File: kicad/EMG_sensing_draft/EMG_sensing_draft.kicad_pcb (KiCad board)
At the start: 2 copper layers, 49.4 x 60.1 mm, 157 parts, among them J1 USB_A_0480370001, J2 Conn_01x09, J3 DEBUG, U1 MCP6N11-002E/SN, U10 RP2040, U11 RN4871-I/RM140, U12 MCP1702T-3302E_CB, U13 Opamp_MCP6024T-E/ST, U14 Opamp_MCP6024T-E/ST, U15 Opamp_MCP6024T-E/ST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

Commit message: Fix layout issues
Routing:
- net Net-(R1-Pad1): track 38.4 -> 40.8 mm
- net GND: track 449.5 -> 450.9 mm
- net Net-(R68-Pad2): track 4.48 -> 5.39 mm
- net Net-(R67-Pad2): track 4.40 -> 5.24 mm
- net Net-(R25-Pad2): track 7.58 -> 8.40 mm
- net Net-(D13-Pad1): track 4.76 -> 5.54 mm
- net Net-(C28-Pad2): track 9.40 -> 8.63 mm
- net Net-(D13-Pad2): track 6.58 -> 7.26 mm
- net +1.65V: track 253.1 -> 253.8 mm
- net Net-(C36-Pad2): track 16.5 -> 17.1 mm

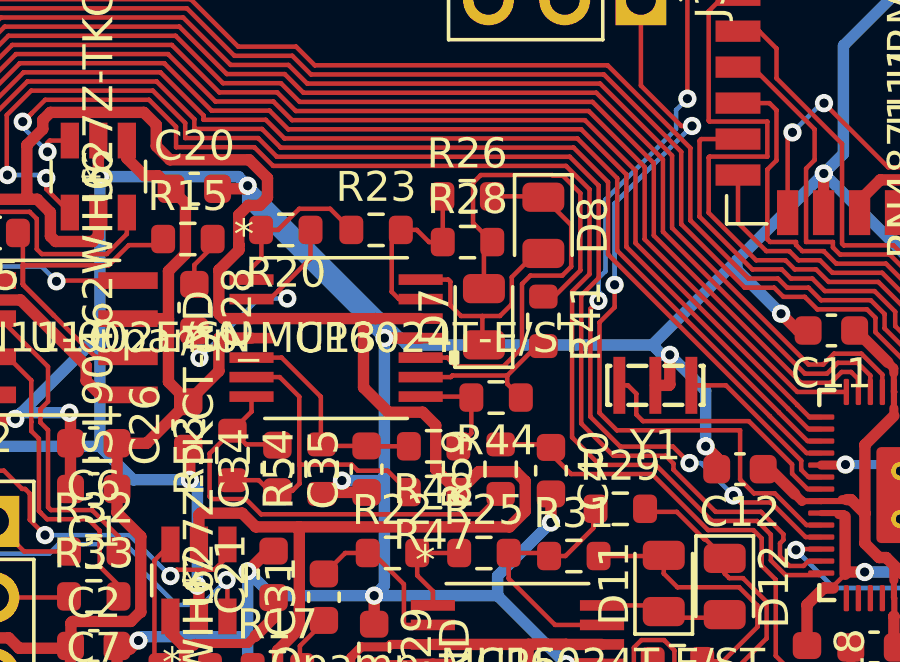
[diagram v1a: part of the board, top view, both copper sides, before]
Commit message: removed references from silkscreen
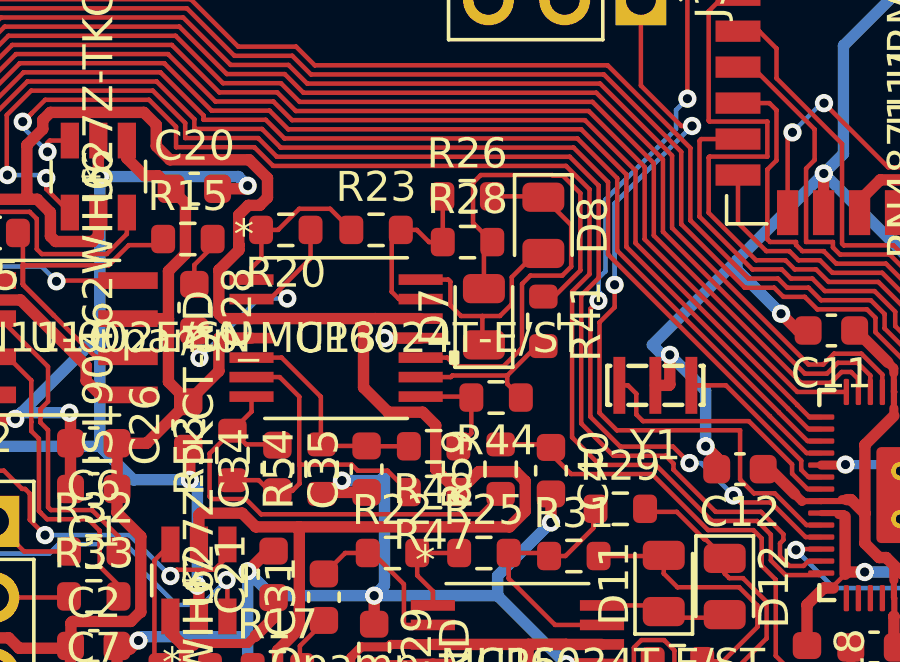
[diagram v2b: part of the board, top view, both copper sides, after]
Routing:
- net GND: track 450.9 -> 423.7 mm
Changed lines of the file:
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@@
   (segment (start 247.0404 47.3964) (end 245.2624 49.1744) (width 0.381) (layer "B.Cu") (net 2))
   (segment (start 243.083746 63.186665) (end 242.297347 62.400266) (width 0.381) (layer "B.Cu") (net 2))
-  (segment (start 242.23842 41.4777) (end 236.93076 36.17004) (width 0.381) (layer "B.Cu") (net 2))
   (segment (start 241.1476 49.8348) (end 241.49 49.4924) (width 0.381) (layer "B.Cu") (net 2))
   (segment (start 268.0716 44.0944) (end 264.4648 44.0944) (width 0.381) (layer "B.Cu") (net 2))
@@
   (segment (start 229.1847 43.942) (end 231.6231 41.5036) (width 0.381) (layer "B.Cu") (net 2))
   (segment (start 233.289299 51.330407) (end 233.413306 51.2064) (width 0.381) (layer "B.Cu") (net 2))
-  (segment (start 241.49 45.8592) (end 241.49 41.2496) (width 0.381) (layer "B.Cu") (net 2))
   (segment (start 251.0028 41.8084) (end 250.7498 41.8084) (width 0.381) (layer "B.Cu") (net 2))
   (segment (start 247.0404 53.4416) (end 247.9548 52.5272) (width 0.3048) (layer "B.Cu") (net 2))
@@
   (segment (start 253.238 38.6588) (end 250.4191 41.4777) (width 0.381) (layer "B.Cu") (net 2))
   (segment (start 233.4768 64.2869) (end 236.5629 64.2869) (width 0.381) (layer "B.Cu") (net 2))
-  (segment (start 250.4191 41.4777) (end 242.23842 41.4777) (width 0.381) (layer "B.Cu") (net 2))
-  (segment (start 241.49 41.2496) (end 236.93076 36.69036) (width 0.381) (layer "B.Cu") (net 2))
   (segment (start 233.413306 51.2064) (end 236.9312 51.2064) (width 0.381) (layer "B.Cu") (net 2))
   (segment (start 235.2548 49.5041) (end 235.2548 46.228) (width 0.381) (layer "B.Cu") (net 2))
@@
   (segment (start 269.5956 78.6892) (end 249.8852 78.6892) (width 0.381) (layer "B.Cu") (net 2))
   (segment (start 265.43 51.9684) (end 268.0716 49.3268) (width 0.381) (layer "B.Cu") (net 2))
-  (segment (start 236.93076 36.69036) (end 236.93076 36.17004) (width 0.381) (layer "B.Cu") (net 2))
   (segment (start 235.2548 46.228) (end 235.0008 45.974) (width 0.381) (layer "B.Cu") (net 2))
   (segment (start 262.9239 48.282) (end 262.404 48.282) (width 0.2032) (layer "F.Cu") (net 3))
@@
   (segment (start 246.933001 74.822601) (end 245.384733 74.822601) (width 0.1524) (layer "F.Cu") (net 140))
   (segment (start 243.4336 73.257801) (end 242.758598 72.582799) (width 0.1524) (layer "F.Cu") (net 140))
-  (zone (net 2) (net_name "GND") (layer "B.Cu") (hatch edge 0.508)
+  (zone locked (net 2) (net_name "GND") (layer "B.Cu") (hatch edge 0.508)
     (connect_pads (clearance 0.508))
     (min_thickness 0.254) (filled_areas_thickness no)

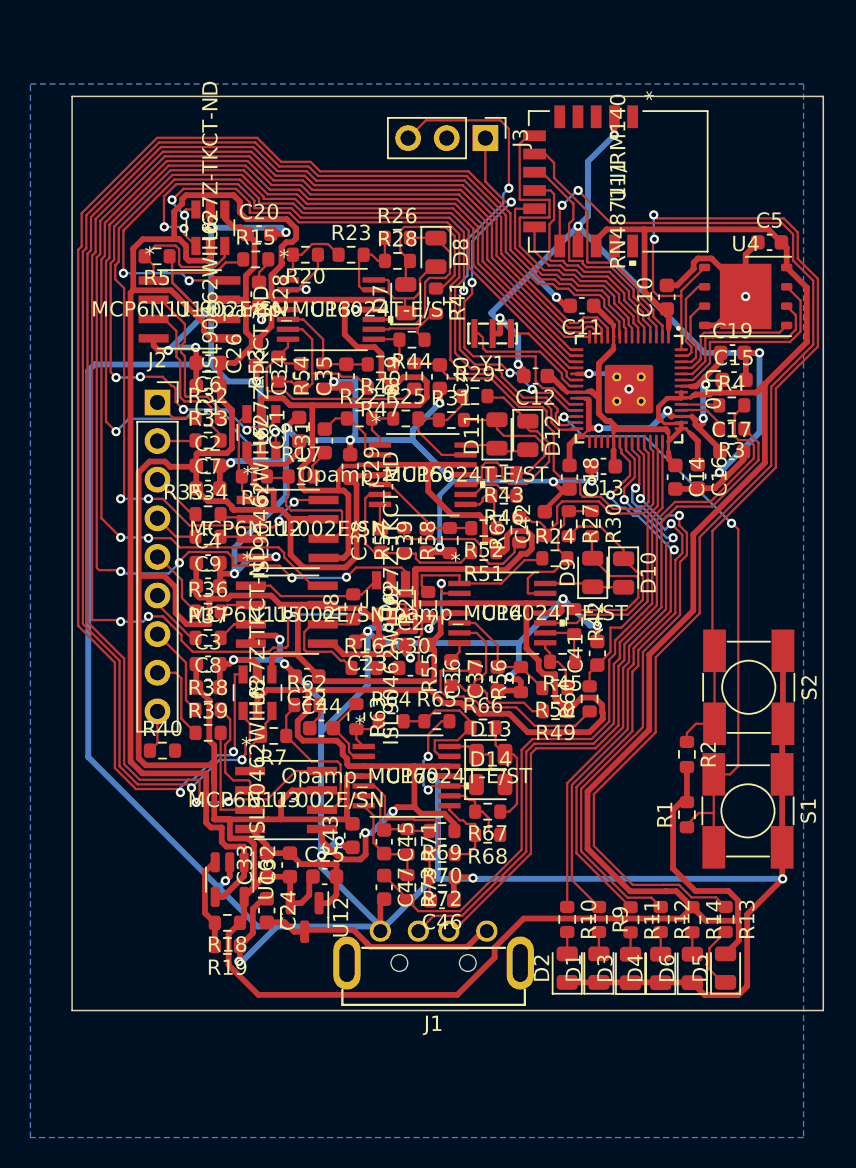
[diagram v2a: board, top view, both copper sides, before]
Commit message: removed references
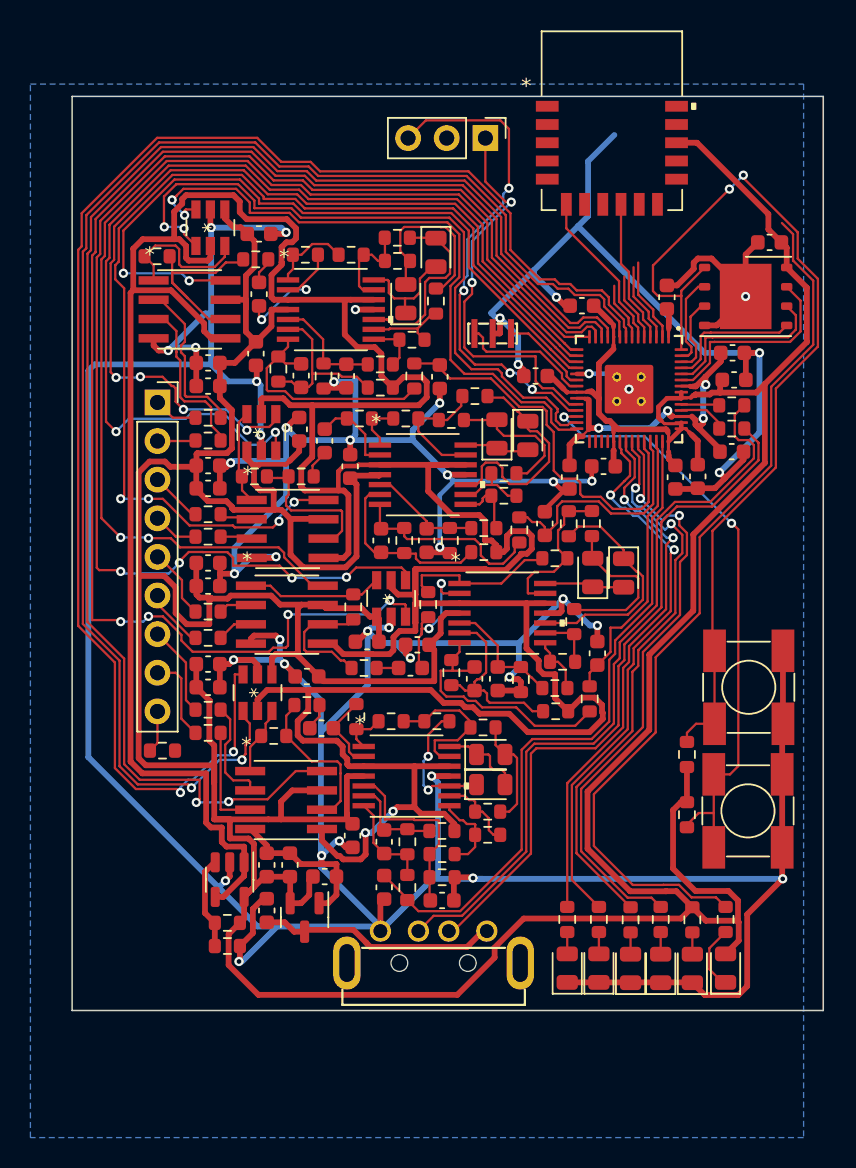
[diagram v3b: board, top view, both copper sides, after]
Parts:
- moved U11 4.01 mm to (258.4, 28.8), turned to 0 degrees
- renumbered J3 to J
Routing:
- net Net-(R13-Pad1): track 76.6 -> 58.1 mm, vias 2 -> 0
- net /RX_IND: track 23.0 -> 10.7 mm
- net /BLE_RX: track 16.9 -> 5.55 mm
- net /RST_N: track 14.8 -> 3.85 mm
- net /BLE_TX: track 16.2 -> 5.20 mm
- net +3.3V: track 357.3 -> 348.2 mm
- net /CTS: track 12.1 -> 4.51 mm
- net /RTS: track 15.5 -> 9.51 mm
- net GND: track 423.7 -> 421.1 mm, vias 44 -> 42

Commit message: finished four layer layout
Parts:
- moved J3 16.8 mm to (233.5, 32.8)
- moved C3 15.5 mm to (241.0, 77.0)
- moved C8 12.1 mm to (240.2, 74.7), turned to -90 degrees
- moved C4 7.47 mm to (235.9, 64.2), turned to 180 degrees
- moved C20 7.23 mm to (228.2, 38.2), turned to 180 degrees
- moved D10 7.01 mm to (253.8, 63.1), turned to 90 degrees
- moved R15 6.81 mm to (228.3, 36.3)
- moved R23 6.80 mm to (234.7, 35.8)
- moved R28 6.66 mm to (237.7, 36.9)
- moved R26 6.63 mm to (237.7, 35.4)
- moved C9 6.62 mm to (238.3, 60.8), turned to -90 degrees
- moved D8 6.50 mm to (241.0, 34.5), turned to 0 degrees
- moved C28 6.05 mm to (231.4, 35.5), turned to 0 degrees
- moved U11 5.99 mm to (253.4, 32.1)
- moved C29 5.93 mm to (237.6, 56.3), turned to 90 degrees
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- renumbered J to J3
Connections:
- U10 pad 11: /DIF_AMP_FOUR_CAL -> Net-(R9-Pad1)
- U10 pad 12: /POT_CHANGE_THREE -> Net-(R10-Pad1)
- U10 pad 13: /POT_CS_THREE -> Net-(R11-Pad1)
- U10 pad 14: /DIF_AMP_THREE_CAL -> Net-(R12-Pad1)
- U10 pad 29: unconnected-(U10-Pad29) -> /DIF_AMP_THREE_CAL
- U10 pad 30: unconnected-(U10-Pad30) -> /POT_CS_THREE
- U10 pad 31: unconnected-(U10-Pad31) -> /POT_CHANGE_THREE
- U10 pad 34: Net-(R9-Pad1) -> unconnected-(U10-Pad34)
- U10 pad 35: Net-(R10-Pad1) -> /DIF_AMP_FOUR_CAL
- U10 pad 36: Net-(R11-Pad1) -> /POT_CS_FOUR
- U10 pad 37: Net-(R12-Pad1) -> /POT_CHANGE_FOUR
- U10 pad 8: /POT_CHANGE_FOUR -> unconnected-(U10-Pad8)
- U10 pad 9: /POT_CS_FOUR -> unconnected-(U10-Pad9)
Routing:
- net GND: track 421.1 -> 114.5 mm, vias 42 -> 40
- net +3.3V: track 348.2 -> 102.3 mm, vias 0 -> 19
- net /POT_CHANGE_THREE: track 94.3 -> 26.1 mm
- net /POT_CS_THREE: track 87.2 -> 23.4 mm
- net +1.65V: track 253.8 -> 192.4 mm
- net /DIF_AMP_THREE_CAL: track 75.8 -> 26.6 mm
- net /DIF_AMP_TWO_CAL: track 71.4 -> 25.4 mm
- net /POT_CHANGE_TWO: track 66.3 -> 22.1 mm
- net /POT_CS_TWO: track 61.8 -> 25.4 mm, vias 4 -> 2
- net Net-(R10-Pad1): track 35.8 -> 56.3 mm
- net Net-(R12-Pad1): track 39.2 -> 59.6 mm
- net Net-(R11-Pad1): track 37.7 -> 58.0 mm
- net Net-(R9-Pad1): track 37.1 -> 56.1 mm
- net Net-(R2-Pad1): track 61.8 -> 43.3 mm
- net /POT_CHANGE_ONE: track 42.6 -> 24.8 mm
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- added copper zone on In2.Cu, net +3.3V
- added copper zone on In1.Cu, net GND
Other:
- copper layers 2 -> 4

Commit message: added silkscreen labels and fixed drc issues
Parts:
- added kibuzzard-63775D6F: G***, kibuzzard-63775D6F, F.Cu at (255.4, 86.7)
- added kibuzzard-63775D95: G***, kibuzzard-63775D95, F.Cu at (257.5, 86.7)
- added kibuzzard-63775DA9: G***, kibuzzard-63775DA9, F.Cu at (259.6, 86.7)
- added kibuzzard-63775DCC: G***, kibuzzard-63775DCC, F.Cu at (261.6, 86.7)
- added kibuzzard-63775DF3: G***, kibuzzard-63775DF3, F.Cu at (263.7, 86.7)
- added kibuzzard-63775E08: G***, kibuzzard-63775E08, F.Cu at (265.8, 86.7)
- added kibuzzard-63775E2B: G***, kibuzzard-63775E2B, F.Cu at (226.6, 52.4)
- added kibuzzard-63775E55: G***, kibuzzard-63775E55, F.Cu at (226.6, 54.8)
- added kibuzzard-63775E69: G***, kibuzzard-63775E69, F.Cu at (226.6, 57.4)
- added kibuzzard-63775E81: G***, kibuzzard-63775E81, F.Cu at (226.6, 59.9)
- added kibuzzard-63775ECF: G***, kibuzzard-63775ECF, F.Cu at (226.6, 62.5)
- added kibuzzard-63775F11: G***, kibuzzard-63775F11, F.Cu at (226.6, 65.0)
- added kibuzzard-63775F30: G***, kibuzzard-63775F30, F.Cu at (226.6, 67.6)
- added kibuzzard-63775F41: G***, kibuzzard-63775F41, F.Cu at (226.6, 70.2)
- added kibuzzard-63775F53: G***, kibuzzard-63775F53, F.Cu at (226.6, 72.6)
- added kibuzzard-63775F9D: G***, kibuzzard-63775F9D, F.Cu at (267.1, 65.2)
- added kibuzzard-63775FC8: G***, kibuzzard-63775FC8, F.Cu at (267.1, 73.5)
- added kibuzzard-63775FF7: G***, kibuzzard-63775FF7, F.Cu at (228.2, 31.0)
- added kibuzzard-63776016: G***, kibuzzard-63776016, F.Cu at (231.0, 31.0)
- added kibuzzard-6377605B: G***, kibuzzard-6377605B, F.Cu at (233.6, 31.0)
- moved C31 0.13 mm to (237.9, 48.6)
- moved D6 0.08 mm to (263.7, 84.6)
- moved D4 0.08 mm to (261.6, 84.6)
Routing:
- net GND: track 114.5 -> 126.4 mm, vias 40 -> 43
- net Net-(C38-Pad1): track 15.7 -> 14.1 mm
- net /DIF_AMP_ONE_CAL: track 48.3 -> 49.7 mm
- net Net-(R64-Pad2): track 7.65 -> 6.71 mm
- net Net-(C36-Pad1): track 16.1 -> 15.4 mm
- net Net-(D13-Pad1): track 12.3 -> 11.7 mm
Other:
- board size 49.4 x 60.1 mm -> 42.6 x 57.1 mm

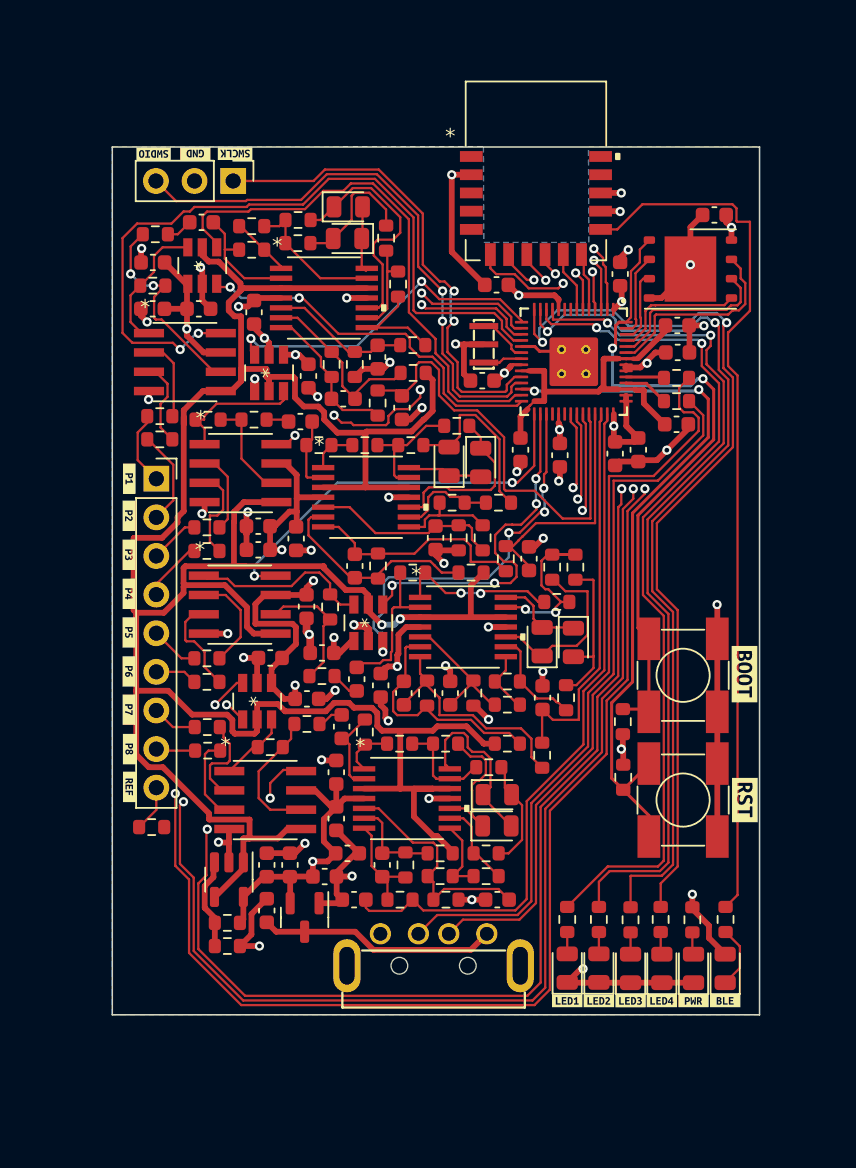
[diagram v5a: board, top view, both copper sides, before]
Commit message: fixed usb mounting
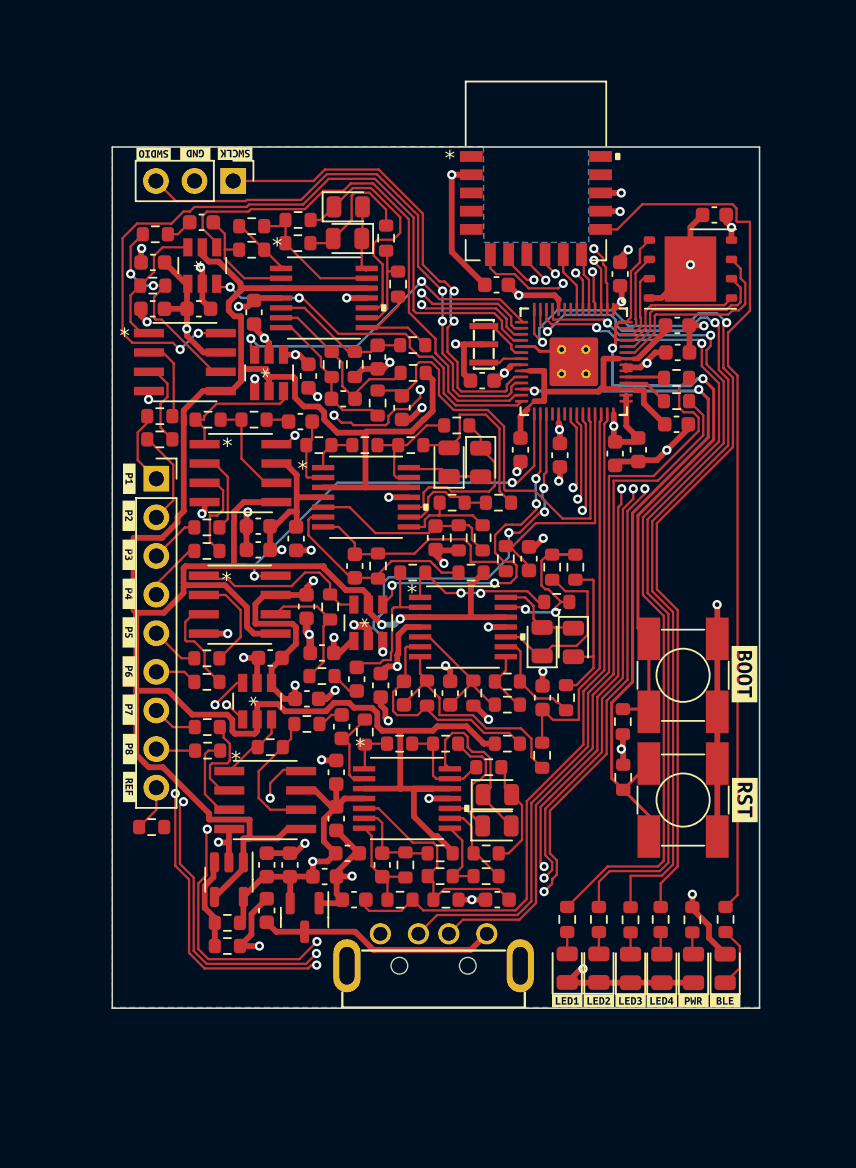
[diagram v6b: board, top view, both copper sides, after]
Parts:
- moved D11 0.05 mm to (247.7, 51.3)
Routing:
- net /DIF_AMP_FOUR_CAL: track 83.7 -> 77.6 mm, vias 4 -> 6
- net /POT_CS_FOUR: track 89.3 -> 83.6 mm, vias 4 -> 6
- net /POT_CHANGE_FOUR: track 93.0 -> 87.8 mm, vias 4 -> 6
- net Net-(D11-Pad2): track 11.9 -> 12.4 mm
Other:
- board size 42.6 x 57.1 mm -> 42.6 x 56.6 mm
